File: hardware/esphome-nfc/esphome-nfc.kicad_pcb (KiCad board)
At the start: 2 copper layers, 11 parts, among them U1 ESP32-C3-WROOM-02, U2 PN7160A1HN/C100Y

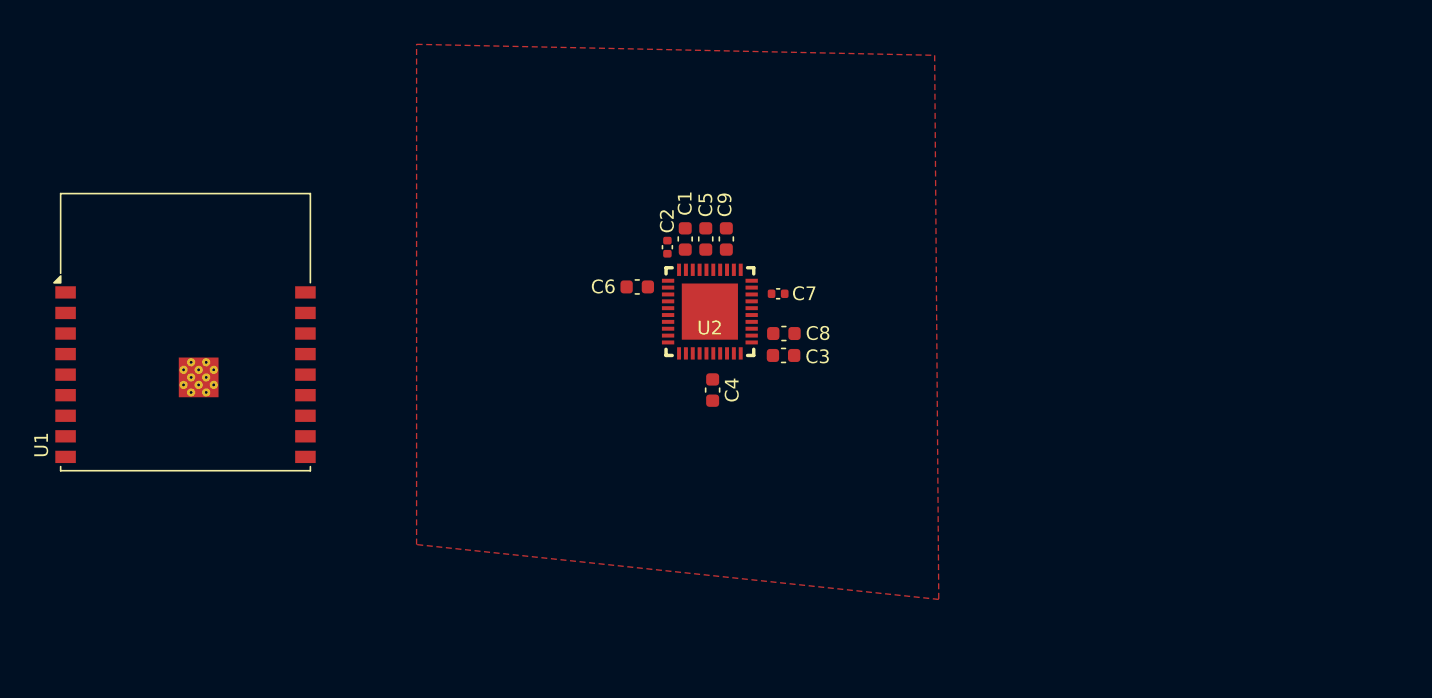
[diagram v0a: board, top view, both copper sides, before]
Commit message: Work in progress on esphome-nfc board
* Done power and clock circuit for PN7160
* Drafted the board dimensions
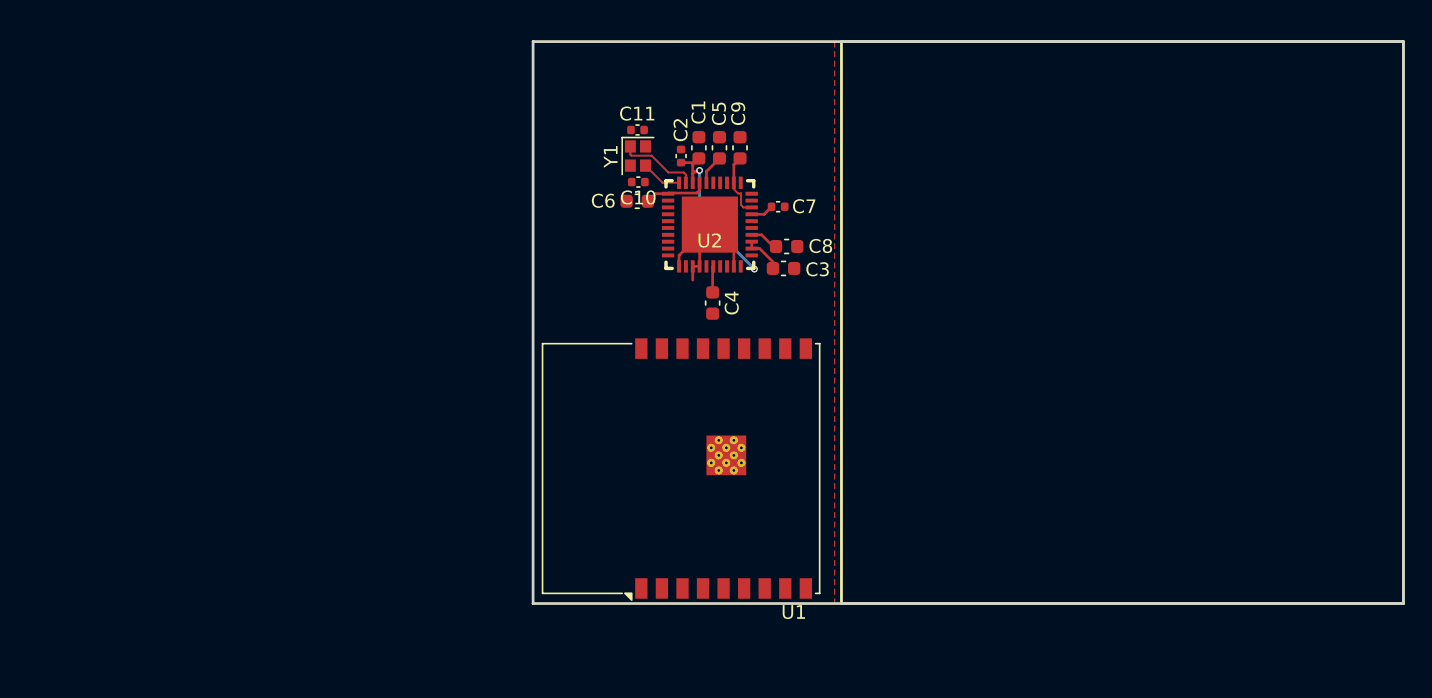
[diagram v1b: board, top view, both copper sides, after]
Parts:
- added C10: 10 pF, Capacitor_SMD:C_0402_1005Metric, F.Cu at (168.7, 84.2)
- added C11: 10 pF, Capacitor_SMD:C_0402_1005Metric, F.Cu at (168.6, 80.5)
- added Y1: Crystal_GND24, Crystal:Crystal_SMD_2016-4Pin_2.0x1.6mm, F.Cu at (168.7, 82.3)
- moved U1 39.9 mm to (174.9, 105.2), turned to 90 degrees
- moved C1 6.72 mm to (173.1, 81.8)
- moved C2 6.72 mm to (171.8, 82.3)
- moved C5 6.72 mm to (174.6, 81.8)
- moved C9 6.72 mm to (176.1, 81.8)
- moved C8 6.35 mm to (179.5, 89.0)
- moved C3 6.35 mm to (179.3, 90.5)
- moved C7 6.35 mm to (178.9, 86.0)
- moved U2 6.35 mm to (173.9, 87.3)
- moved C4 6.35 mm to (174.1, 93.1)
- moved C6 6.25 mm to (168.6, 85.7)
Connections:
- C1 pad 1: /TODO3 -> +5V
- C2 pad 1: /TODO3 -> +5V
- C3 pad 1: /TODO2 -> +5V
- C4 pad 1: /TODO1 -> +3V3
- U2 pad 12: /TODO3 -> +5V
- U2 pad 13: /TODO2 -> +5V
- U2 pad 28: /TODO3 -> +5V
- U2 pad 29: unconnected-(U2-XTAL2-Pad29) -> /XTAL2
- U2 pad 30: unconnected-(U2-NFC_CLK_XTAL1-Pad30) -> /XTAL1
- U2 pad 41: unconnected-(U2-VSS-Pad41) -> GND
- U2 pad 6: /TODO1 -> +3V3
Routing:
- net +5V: track 0.00 -> 15.8 mm, vias 0 -> 2
- net GND: track 0.00 -> 12.6 mm
- net Net-(U2-VDD(A)): track 0.00 -> 6.82 mm
- net /TVDD: track 0.00 -> 6.70 mm
- net /XTAL2: track 0.00 -> 5.84 mm
- net /XTAL1: track 0.00 -> 2.97 mm
- net +3V3: track 0.00 -> 1.92 mm
- net Net-(U2-VDD(VMID)): track 0.00 -> 1.68 mm
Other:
- board outline added: 63.5 x 41 mm
- copper layers 2 -> 4

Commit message: Work in progress on esphome-nfc board
* Routed most of things related to the USB
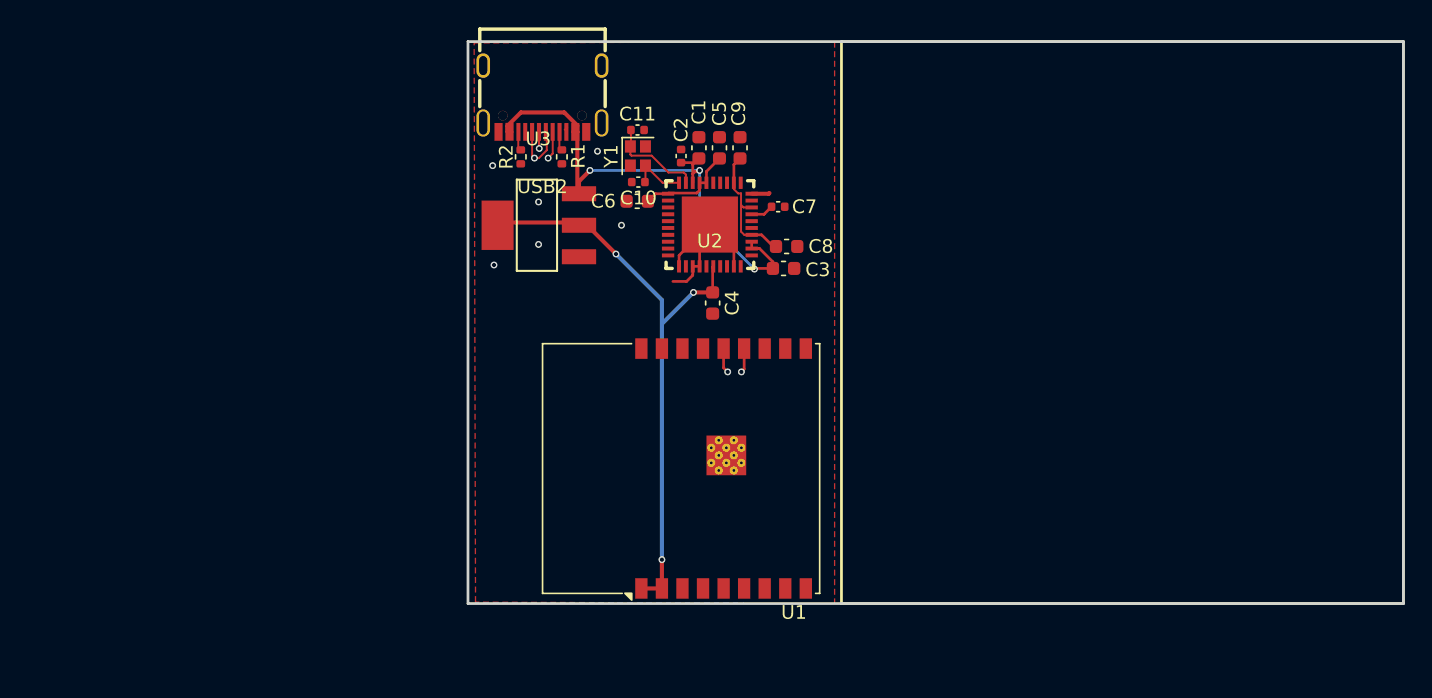
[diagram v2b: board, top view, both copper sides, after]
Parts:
- added R1: 5.1K, Resistor_SMD:R_0402_1005Metric, F.Cu at (163.1, 82.4)
- added R2: 5.1K, Resistor_SMD:R_0402_1005Metric, F.Cu at (160.1, 82.4)
- added U3: AMS1117-3.3, easyeda2kicad:SOT-223-3_L6.5-W3.4-P2.30-LS7.0-BR, F.Cu at (161.4, 87.4)
- added USB2: KH-TYPE-C-16P, easyeda2kicad:USB-C-SMD_KH-TYPE-C-16P, F.Cu at (161.7, 78.2)
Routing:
- net +3V3: track 1.92 -> 43.5 mm, vias 0 -> 3
- net /D+: track 0.00 -> 28.0 mm, vias 0 -> 2
- net /D-: track 0.00 -> 27.5 mm, vias 0 -> 3
- net +5V: track 15.8 -> 38.9 mm, vias 2 -> 3
- net GND: track 12.6 -> 15.8 mm, vias 0 -> 6
- net /TVDD: track 6.70 -> 9.52 mm
- net /XTAL2: track 5.84 -> 7.06 mm
- net /XTAL1: track 2.97 -> 4.18 mm
- net Net-(USB2-CC2): track 0.00 -> 1.16 mm
- net Net-(USB2-CC1): track 0.00 -> 1.16 mm
- net Net-(U2-VDD(A)): track 6.82 -> 7.32 mm
- added copper zone on In1.Cu, net GND
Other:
- board size 63.5 x 41 mm -> 68.2 x 41 mm

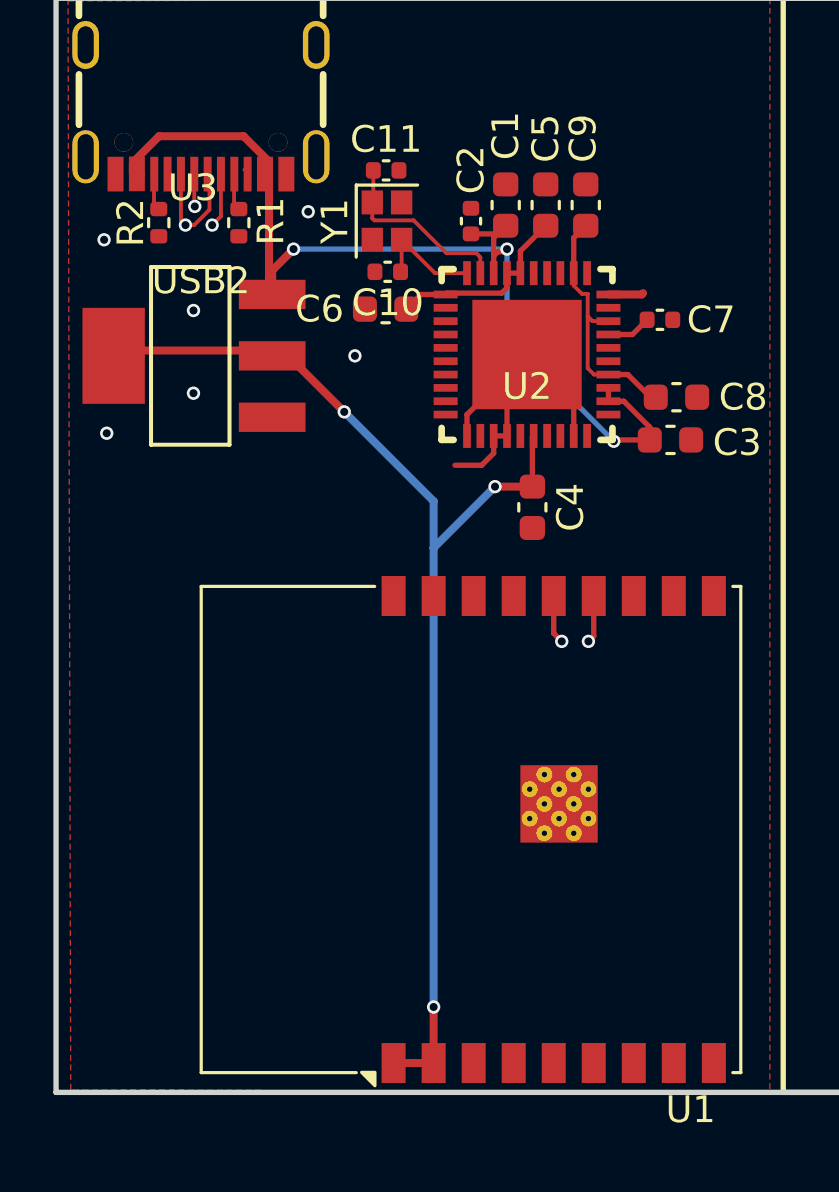
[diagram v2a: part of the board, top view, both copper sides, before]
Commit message: Route MCU <--> NFC chip connections
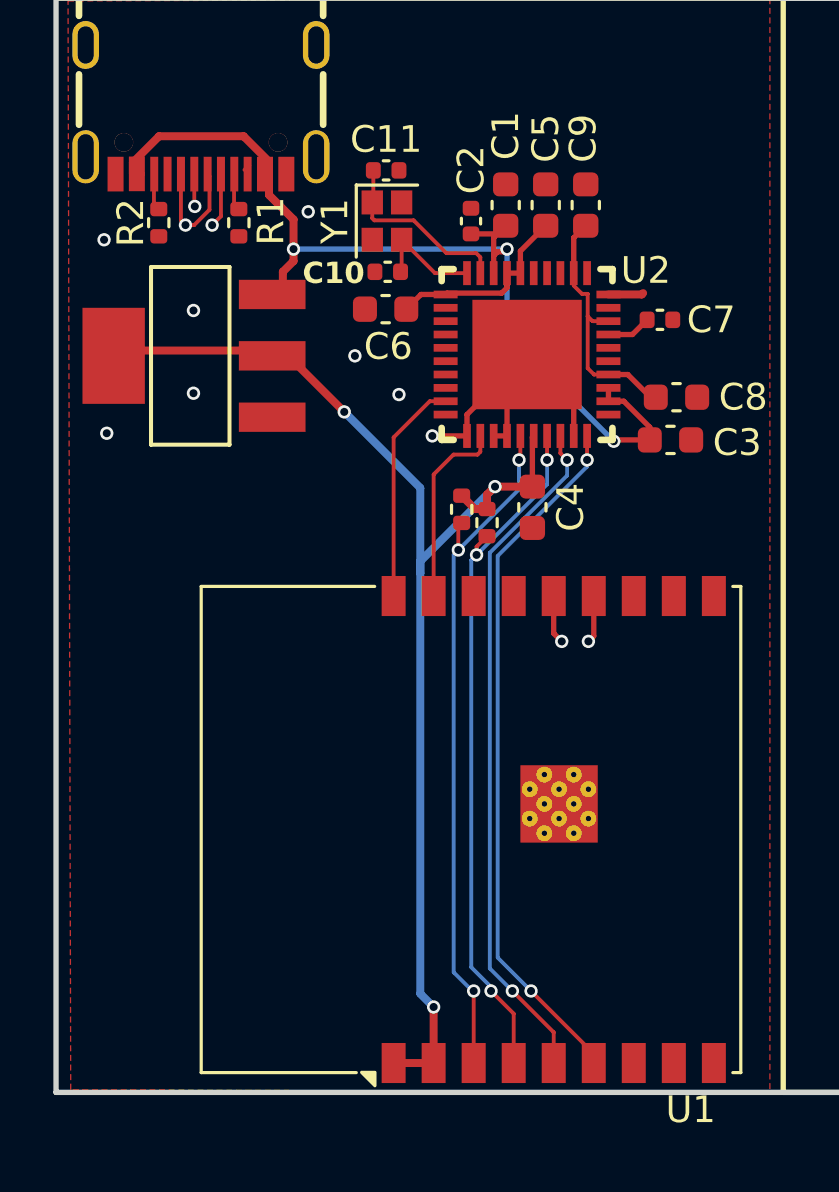
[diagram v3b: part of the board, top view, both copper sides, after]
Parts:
- added R3: 10k, Resistor_SMD:R_0402_1005Metric, F.Cu at (171.4, 93.2)
- added R4: 10k, Resistor_SMD:R_0402_1005Metric, F.Cu at (172.4, 93.7)
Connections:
- U1 pad 17: unconnected-(U1-IO1-Pad17) -> /NFC_DWL
- U1 pad 18: unconnected-(U1-IO0-Pad18) -> /NFC_WKUP
- U1 pad 3: unconnected-(U1-IO4-Pad3) -> /NFC_SDA
- U1 pad 4: unconnected-(U1-IO5-Pad4) -> /NFC_SCL
- U1 pad 5: unconnected-(U1-IO6-Pad5) -> /NFC_IRQ
- U1 pad 6: unconnected-(U1-IO7-Pad6) -> /NFC_VEN
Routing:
- net /NFC_VEN: track 0.00 -> 26.4 mm, vias 0 -> 2
- net /NFC_SCL: track 0.00 -> 26.2 mm, vias 0 -> 3
- net /NFC_SDA: track 0.00 -> 25.9 mm, vias 0 -> 3
- net /NFC_IRQ: track 0.00 -> 25.8 mm, vias 0 -> 2
- net /NFC_WKUP: track 0.00 -> 8.46 mm
- net /NFC_DWL: track 0.00 -> 7.25 mm
- net +3V3: track 43.5 -> 46.7 mm
- net +5V: track 38.9 -> 37.8 mm
- net GND: track 15.8 -> 14.8 mm, vias 6 -> 8

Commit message: Fix DRC errors
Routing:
- net GND: track 14.8 -> 16.1 mm
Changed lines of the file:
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@@
 			(at -0.14 -0.35 90)
 			(size 0.6 0.6)
-			(drill 0.2)
+			(drill 0.3)
 			(property pad_prop_heatsink)
 			(layers "*.Cu" "F.Mask")
@@
 			(at -0.14 0.75 90)
 			(size 0.6 0.6)
-			(drill 0.2)
+			(drill 0.3)
 			(property pad_prop_heatsink)
 			(layers "*.Cu" "F.Mask")
@@
 			(at 0.41 -0.9 90)
 			(size 0.6 0.6)
-			(drill 0.2)
+			(drill 0.3)
 			(property pad_prop_heatsink)
 			(layers "*.Cu" "F.Mask")
@@
 			(at 0.41 0.2 90)
 			(size 0.6 0.6)
-			(drill 0.2)
+			(drill 0.3)
 			(property pad_prop_heatsink)
 			(layers "*.Cu" "F.Mask")
@@
 			(at 0.41 1.3 90)
 			(size 0.6 0.6)
-			(drill 0.2)
+			(drill 0.3)
 			(property pad_prop_heatsink)
 			(layers "*.Cu" "F.Mask")
@@
 			(at 0.96 -0.35 90)
 			(size 0.6 0.6)
-			(drill 0.2)
+			(drill 0.3)
 			(property pad_prop_heatsink)
 			(layers "*.Cu" "F.Mask")
@@
 			(at 0.96 0.75 90)
 			(size 0.6 0.6)
-			(drill 0.2)
+			(drill 0.3)
 			(property pad_prop_heatsink)
 			(layers "*.Cu" "F.Mask")
@@
 			(at 1.51 -0.9 90)
 			(size 0.6 0.6)
-			(drill 0.2)
+			(drill 0.3)
 			(property pad_prop_heatsink)
 			(layers "*.Cu" "F.Mask")
@@
 			(at 1.51 0.2 90)
 			(size 0.6 0.6)
-			(drill 0.2)
+			(drill 0.3)
 			(property pad_prop_heatsink)
 			(layers "*.Cu" "F.Mask")
@@
 			(at 1.51 1.3 90)
 			(size 0.6 0.6)
-			(drill 0.2)
+			(drill 0.3)
 			(property pad_prop_heatsink)
 			(layers "*.Cu" "F.Mask")
@@
 			(at 2.06 -0.35 90)
 			(size 0.6 0.6)
-			(drill 0.2)
+			(drill 0.3)
 			(property pad_prop_heatsink)
 			(layers "*.Cu" "F.Mask")
@@
 			(at 2.06 0.75 90)
 			(size 0.6 0.6)
-			(drill 0.2)
+			(drill 0.3)
 			(property pad_prop_heatsink)
 			(layers "*.Cu" "F.Mask")
@@
 	)
 	(segment
+		(start 164.94 80.79)
+		(end 165.86 81.71)
+		(width 0.3)
+		(layer "F.Cu")
+		(net 1)
+	)
+	(segment
 		(start 172.65 90.4)
 		(end 173.15 90.4)
@@
 	)
 	(via
+		(at 165.9 81.75)
+		(size 0.5)
+		(drill 0.3)
+		(layers "F.Cu" "B.Cu")
+		(free yes)
+		(net 1)
+	)
+	(via
 		(at 167.45 87.4)
 		(size 0.5)
@@
 		(size 0.5)
 		(drill 0.3)
-		(layers "F.Cu" "B.Cu")
-		(free yes)
-		(net 1)
-	)
-	(via
-		(at 165.7 82)
-		(size 0.5)
-		(drill 0.3)

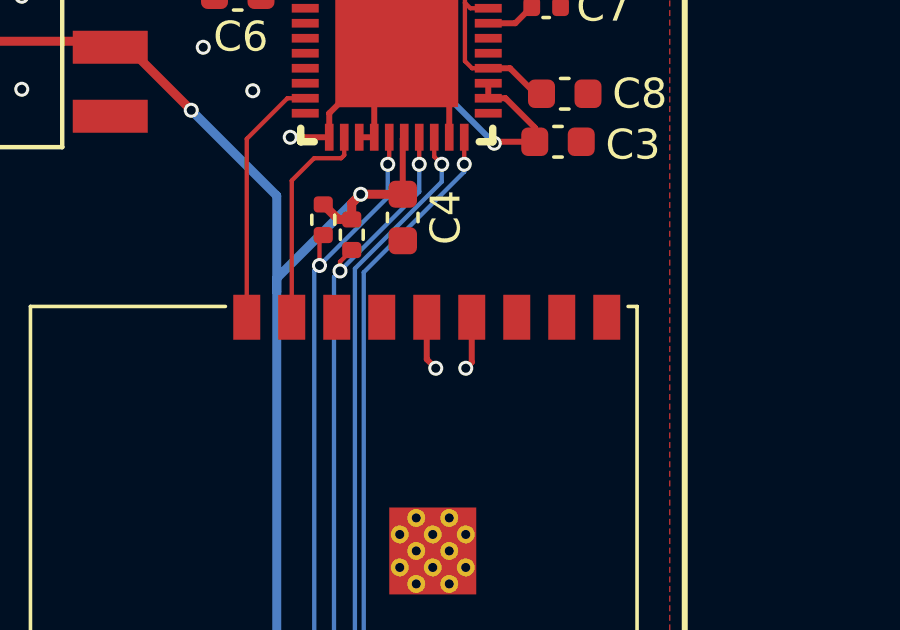
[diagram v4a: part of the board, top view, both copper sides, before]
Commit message: Re-route D+/D- using differential pair tools
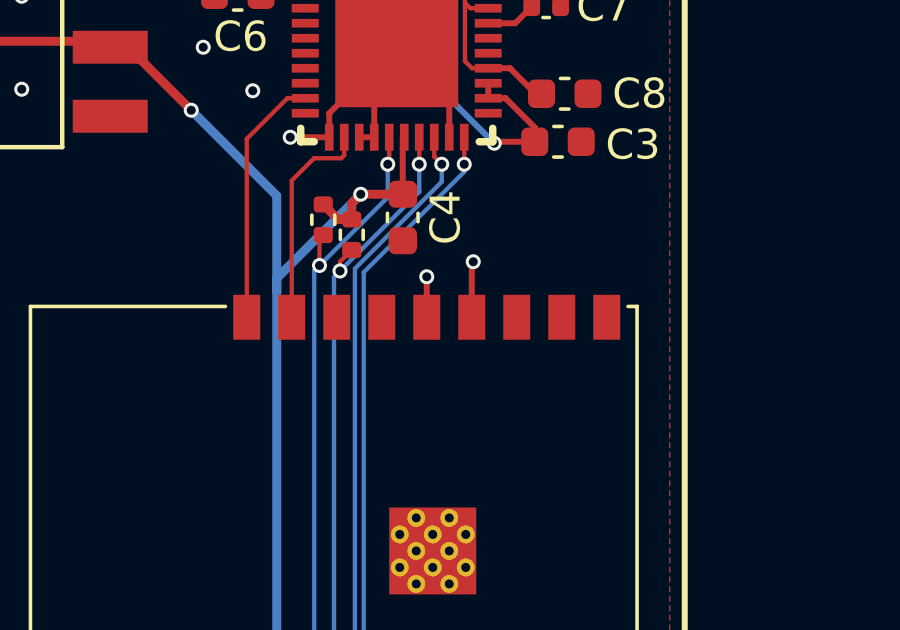
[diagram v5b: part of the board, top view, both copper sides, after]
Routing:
- net /D+: track 28.0 -> 26.1 mm
- net /D-: track 27.5 -> 25.9 mm
